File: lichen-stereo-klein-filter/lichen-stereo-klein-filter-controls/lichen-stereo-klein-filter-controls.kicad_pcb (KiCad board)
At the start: 2 copper layers, 29 x 108 mm, 39 parts, among them J1 Thonkiconn_Mono_Audio_Jack, J2 Thonkiconn_Mono_Audio_Jack, J3 Thonkiconn_Mono_Audio_Jack, J4 Thonkiconn_Mono_Audio_Jack, J5 Thonkiconn_Mono_Audio_Jack, J6 Thonkiconn_Mono_Audio_Jack, J7 Conn_02x07_Top_Bottom, U1 TL074

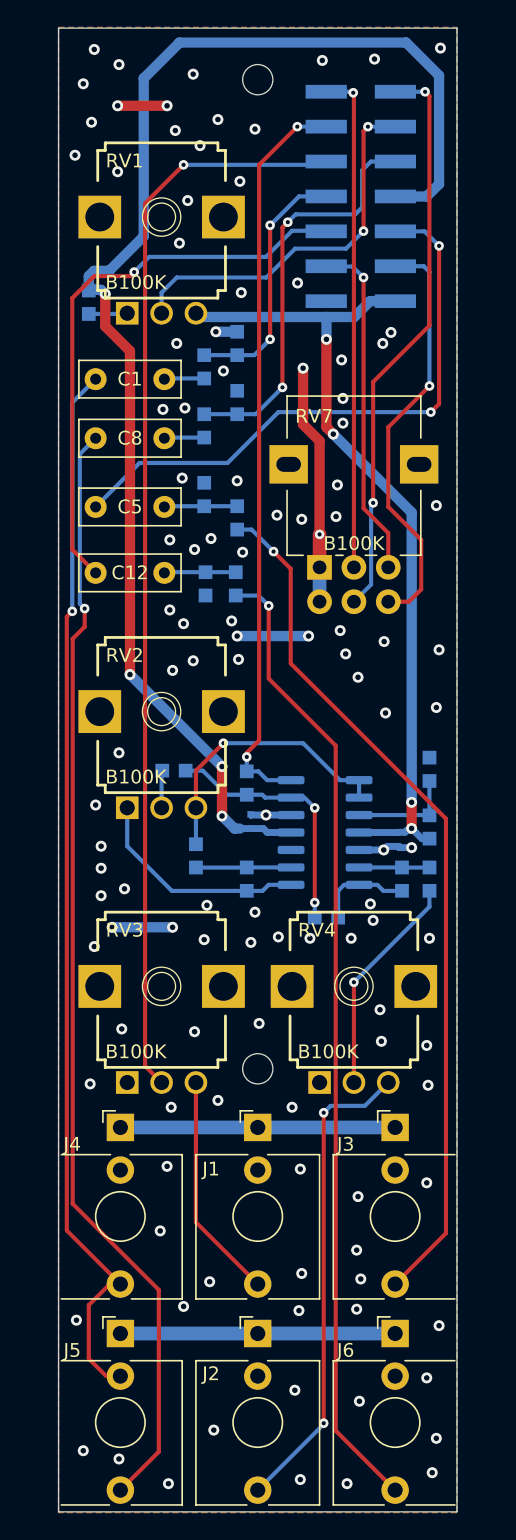
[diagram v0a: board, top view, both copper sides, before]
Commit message: feat: Updates Crustose, Cladonia and YouMe Transformer. Adds Stereo Latencies.
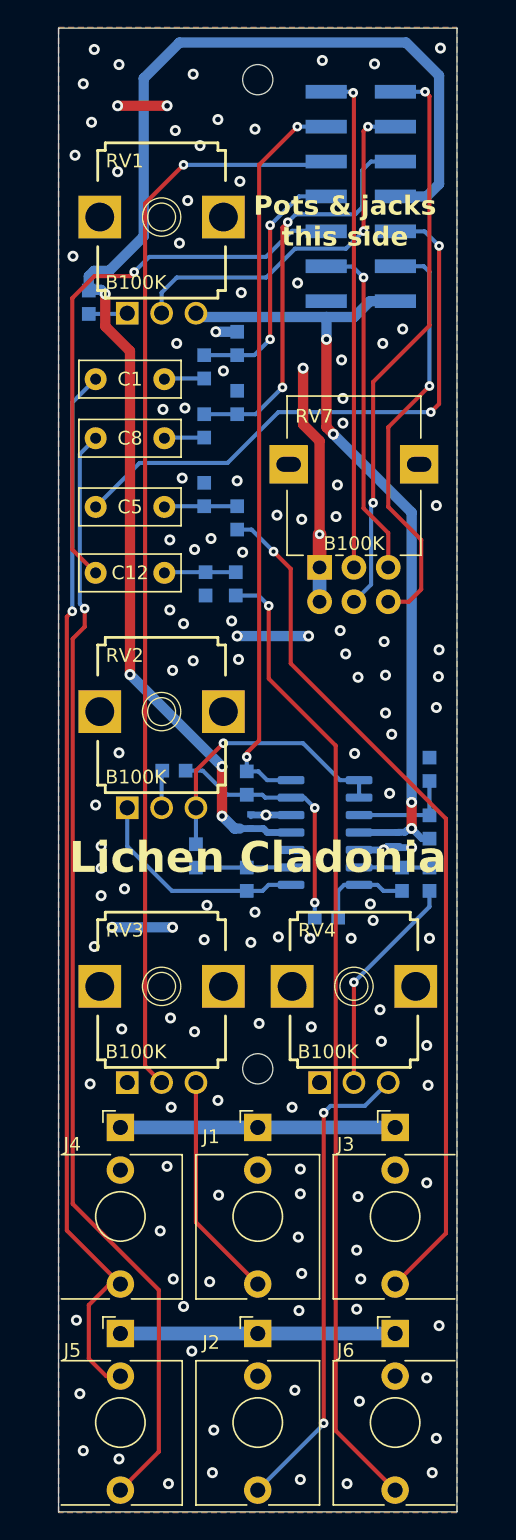
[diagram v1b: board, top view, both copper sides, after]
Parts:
- J7: value Conn_02x07_Top_Bottom -> 02x07 Socket
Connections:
- net AUDIO_OUT_UNFILTERED_L renamed AUDIO_OUT_DC_COUPLED_L
- net AUDIO_OUT_UNFILTERED_R renamed AUDIO_OUT_DC_COUPLED_R
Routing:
- net GND: vias 117 -> 132
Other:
- board text added: "Cladonia control board v1.0 © 2026, Colin Clark"
- board text added: "Lichen Cladonia"
- board text added: "Pots & jacks this side"
